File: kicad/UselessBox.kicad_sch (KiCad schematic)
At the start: 21 parts, among them J1 Screw_Terminal_01x02, J2 Screw_Terminal_01x02, J4 Servo, Q1 IRF9540N, Q2 BC548, SW1 DPDT, U1 NE555P, U2 NE555P

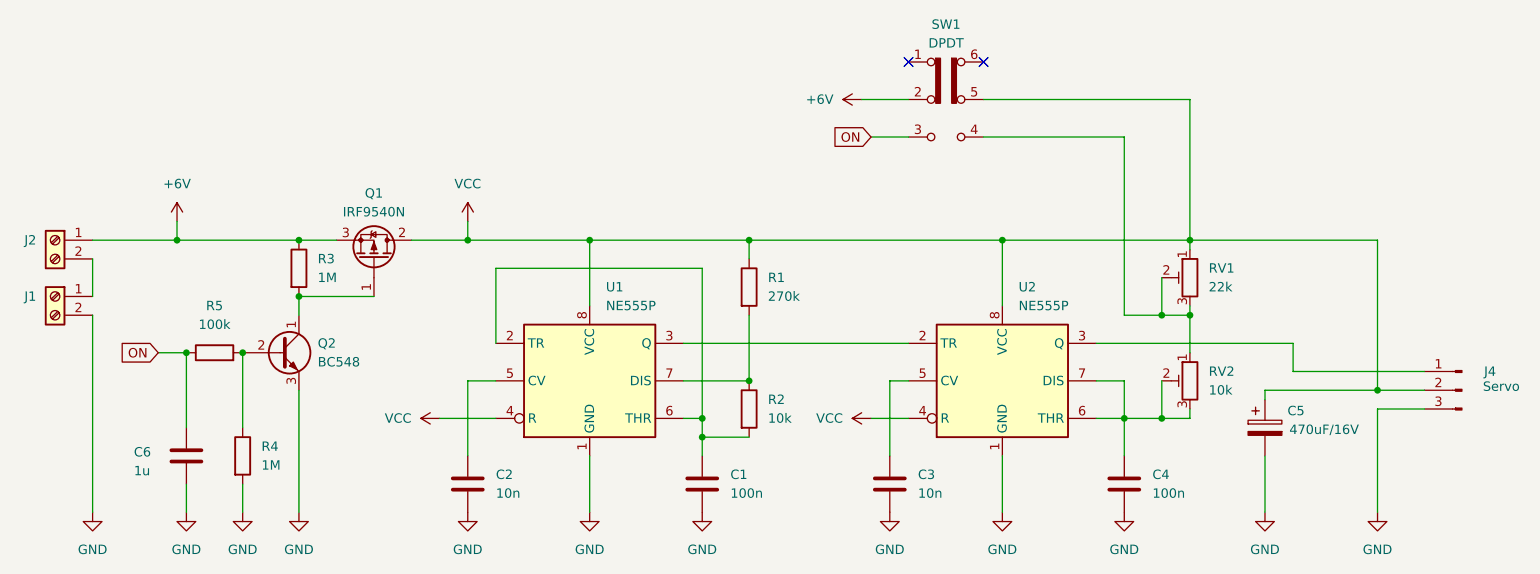
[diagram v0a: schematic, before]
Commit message: Turn-on jumper added
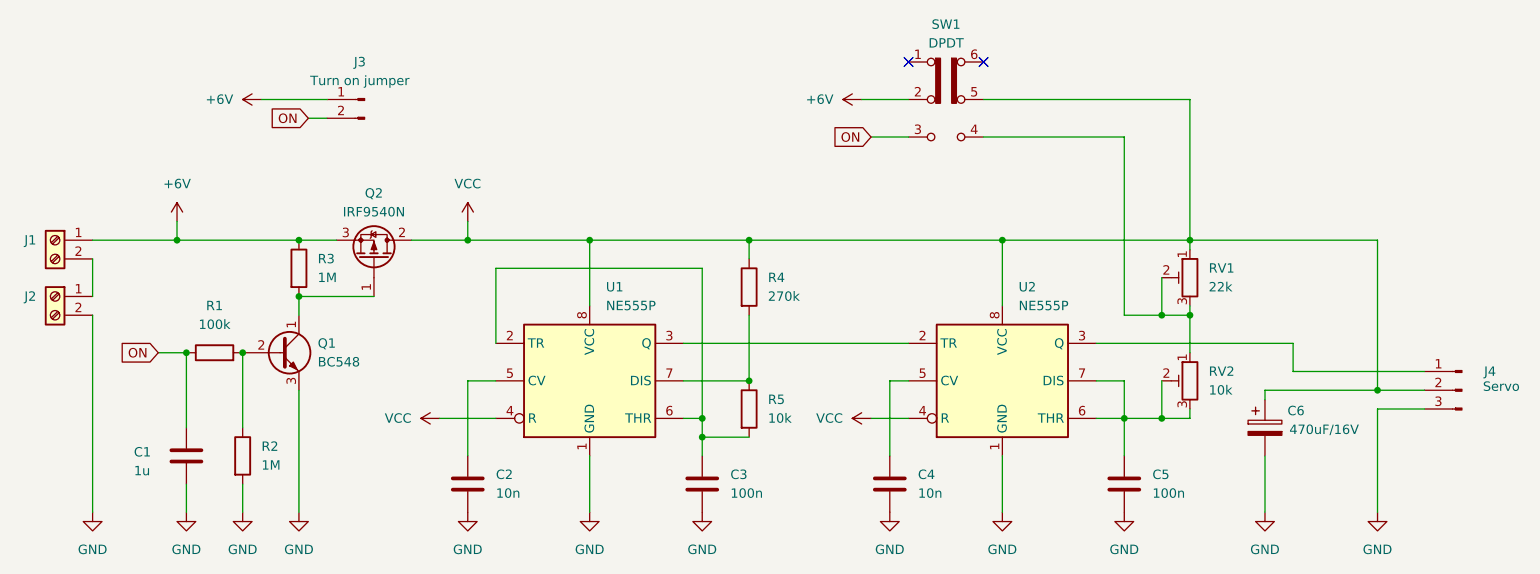
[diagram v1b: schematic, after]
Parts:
- added J3: Turn on jumper, Connector_PinHeader_2.54mm:PinHeader_1x02_P2.54mm_Vertical, symbol Connector:Conn_01x02_Pin
- renumbered C6 to C1, C1 to C3, C3 to C4, C4 to C5, C5 to C6, J2 to J1, J1 to J2, Q2 to Q1, Q1 to Q2, R5 to R1, R4 to R2, R1 to R4, R2 to R5
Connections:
- net +6V: now also J3.1 (Pin_1)
- net ON: now also J3.2 (Pin_2)
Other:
- company: (none) -> www.elektrokrouzek.cz
- title: (none) -> NE555 useless box
